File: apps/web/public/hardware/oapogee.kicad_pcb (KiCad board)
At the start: 2 copper layers, 22 x 60 mm, 27 parts, among them J1 USB-C-16P, J2 S2B-PH-K-S, J3 ANT-902-928, SW1 ARM-SWITCH, U1 MCP73831, U2 TODO-BUCK-BOOST, U3 RP2350A, U4 W25Q128JVSIQ, U5 BMP390, U6 ICM-42688-P, U7 ADXL375, U8 SX1262, U9 MAX-M10S

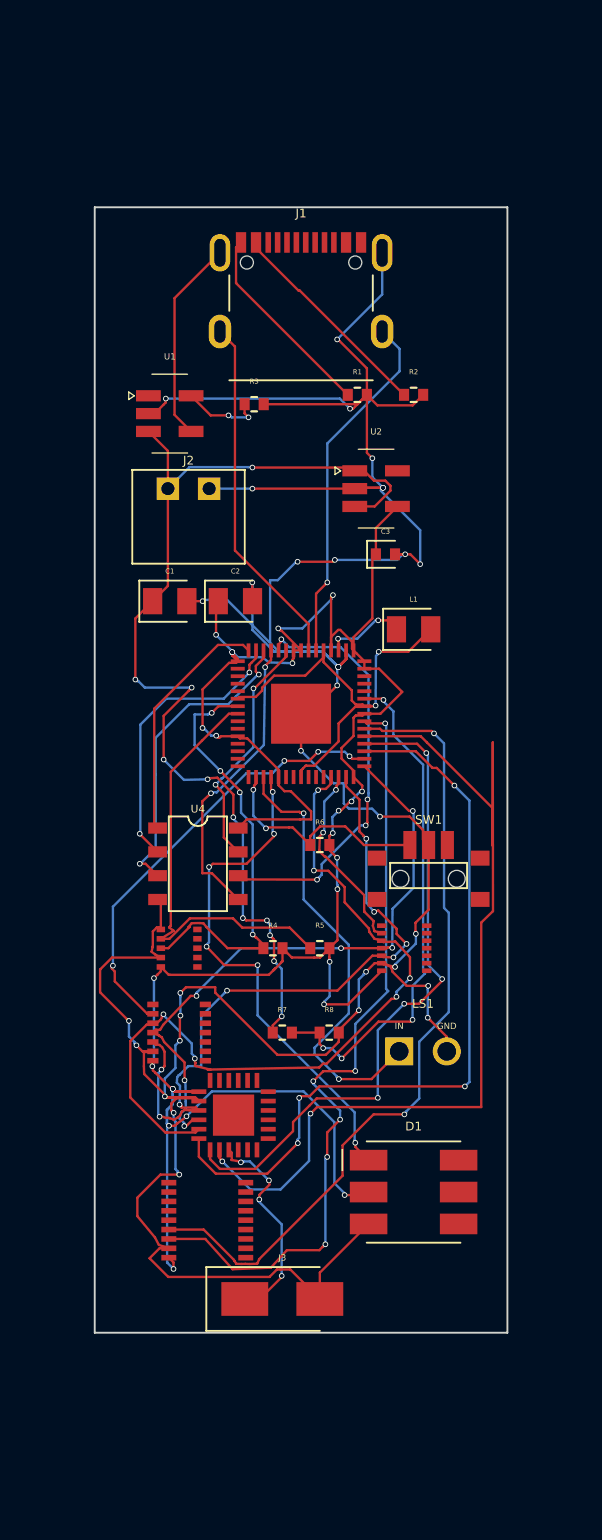
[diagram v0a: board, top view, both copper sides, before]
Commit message: The board could be flashed once and then never again
A page verification pass across the whole site found a hardware defect, which is
not where I expected one to come from.

RUN, SWCLK and SWDIO were all NOT_CONNECTED in the generated netlist, and
QSPI_CS went only to the flash. There is no dedicated bootloader pin on this
microcontroller: holding the flash chip select low as the chip leaves reset is
what selects USB boot. So a fabricated board could have been programmed exactly
once, while its flash was still blank and the bootrom fell through to USB, and
after that there would have been no way into the bootloader, no way to reset it,
and no way to attach a debugger. For a payload meant to be reflashed between
flights that is fatal, and I published Gerbers for it.

It was invisible in the schematic because the pins were simply absent, and
invisible to every check because nothing asserts that a microcontroller can be
programmed. Three pages meanwhile told the reader to "hold the boot button",
which is how it was caught: an instruction referring to a part that does not
exist.

The board now has SW2 on the flash chip select, SW3 on RUN, R9 pulling RUN up,
and three SWD pads. Press and hold boot, tap reset, release boot. It still
routes: 31 components, 108 traces, 152 vias, no missing traces, no unconnected
ports, no placement errors, and the fabrication package regenerated. The build
guide, the firmware page and the troubleshooting entry now describe what those
buttons actually do, including that a blank board enumerates on its own so the
first flash works even with an unsoldered button, which is exactly the sort of
thing that hides a missing part until the second flash.

The schematic page carried a red callout saying the pin numbers were structural
placeholders and "do not send anything here to a fabricator", twenty lines above
a Files tab offering the Gerbers and a heading saying the board can be ordered.
Both cannot be true. The pin numbers stopped being placehold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
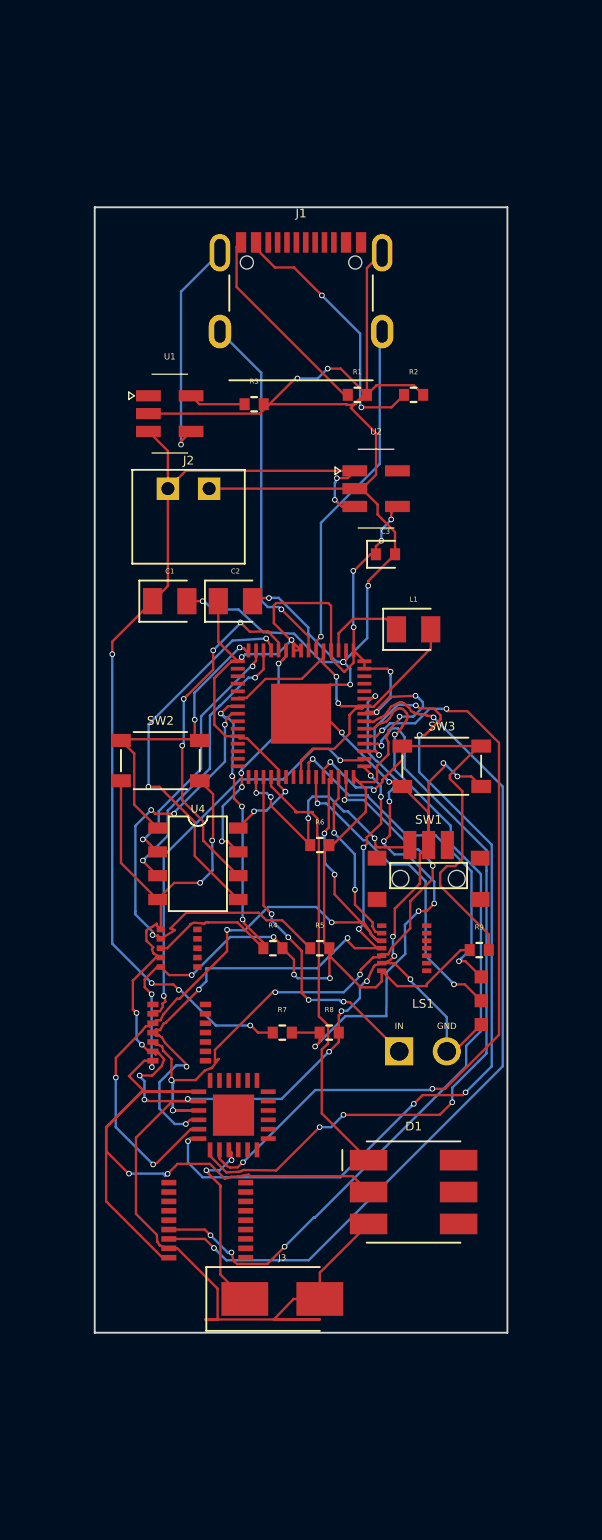
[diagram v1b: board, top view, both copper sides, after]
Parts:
- added J4: SWD-PADS, tscircuit:SWD-PADS, F.Cu at (109.6, 112.3)
- added R9: 10kΩ, tscircuit:resistor_res0402, F.Cu at (109.5, 109.6)
- added SW2: BOOT-BUTTON, tscircuit:BOOT-BUTTON, F.Cu at (92.5, 99.5)
- added SW3: RESET-BUTTON, tscircuit:RESET-BUTTON, F.Cu at (107.5, 99.8)
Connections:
- net .U3 .QSPI_CS to .U4 .CS renamed .SW2 .A1 to .U3 .QSPI_CS
- U3 pad 24: (no net) -> .J4 .SWCLK to .U3 .SWCLK
- U3 pad 25: (no net) -> .J4 .SWDIO to .U3 .SWDIO
- U3 pad 26: (no net) -> .SW3 .A1 to .U3 .RUN
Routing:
- net .SW3 .A1 to .U3 .RUN: track 0.00 -> 24.9 mm, vias 0 -> 2
- net .J4 .SWCLK to .U3 .SWCLK: track 0.00 -> 18.6 mm, vias 0 -> 2
- net .J4 .SWDIO to .U3 .SWDIO: track 0.00 -> 16.9 mm, vias 0 -> 2
- net V3V3: track 125.5 -> 141.0 mm, vias 24 -> 20
- net .U3 .RADIO_DIO1 to .U8 .DIO1: track 54.0 -> 42.6 mm, vias 2 -> 4
- net .U3 .CS_RADIO to .U8 .NSS: track 40.9 -> 48.4 mm, vias 4 -> 6
- net .U3 .BUZZER to .LS1 .IN: track 23.7 -> 18.8 mm, vias 2 -> 4
- net .U3 .GNSS_RX to .U9 .TXD: track 42.2 -> 47.0 mm, vias 6 -> 2
- net .U3 .RADIO_BUSY to .U8 .BUSY: track 35.6 -> 40.3 mm
- net .U3 .QSPI_D0 to .U4 .DI: track 16.1 -> 20.5 mm
- net .U3 .LED to .D1 .DIN: track 27.7 -> 23.8 mm, vias 6 -> 0
- net .U3 .QSPI_SCK to .U4 .CLK: track 22.6 -> 19.0 mm
- net .SW2 .A1 to .U3 .QSPI_CS: track 13.0 -> 16.5 mm, vias 0 -> 2
- net GND: track 193.5 -> 196.7 mm, vias 34 -> 27
- net VBAT: track 56.5 -> 53.4 mm, vias 11 -> 6
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
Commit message: Choose the regulator, and find out the board had outgrown itself
U2 was manufacturerPartNumber="TODO-BUCK-BOOST" on a five pin SOT-23, which is a
placeholder standing in for the part that feeds everything else. It is a
TPS63001 now, and every figure behind that choice comes from TI's datasheet
SLVS520C rather than from memory: 1.8 V to 5.5 V in, which spans a single
lithium cell from full charge to cutoff; fixed 3.3 V out, so there is no
feedback divider and no resistor pair to get wrong; up to 800 mA; 40 uA typical
quiescent at no load; VSON-10, 3 by 3 mm, exposed pad to PGND; one external
2.2 uH inductor, which is now L2.

Quiescent current decided it rather than efficiency at load. This payload sits
armed on a pad and then beeps in a field, both at almost no draw, so standing
loss is what sets how long it keeps beeping.

The schematic carries the datasheet's own pin numbering, the pad tied to PGND,
FB tied to VOUT as fixed-output parts require, and PS/SYNC grounded to enable
power-save, which is the mode that matters for a payload spending hours near
zero load.

Choosing it exposed something else. Adding eleven pads and two parts to a 22 by
60 mm board took the autorouter from seconds to over ten minutes, and then to
not finishing at all: a run was killed after forty-three minutes still working
on the schematic export. That is not a slow build, it is a build that cannot be
relied on to complete. The board is 28 by 78 mm with the placement spread to
match, which routes in under a minute, and the closest copper improved from
0.108 to 0.115 mm and the closest copper to a board edge from 0.72 to 1.34 mm as
a side effect. 32 components, 115 traces, 153 vias, nothing missing, nothing
unconnected, no placement errors, and the fabrication package regenerated. It
still fits the BT-55 sled, with 1.85 mm of rail each side instead of 0.6.

Also decided: the status LED is three plain LEDs, not an addressable one. The
WS2812 family wants a supply above the only rail this board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
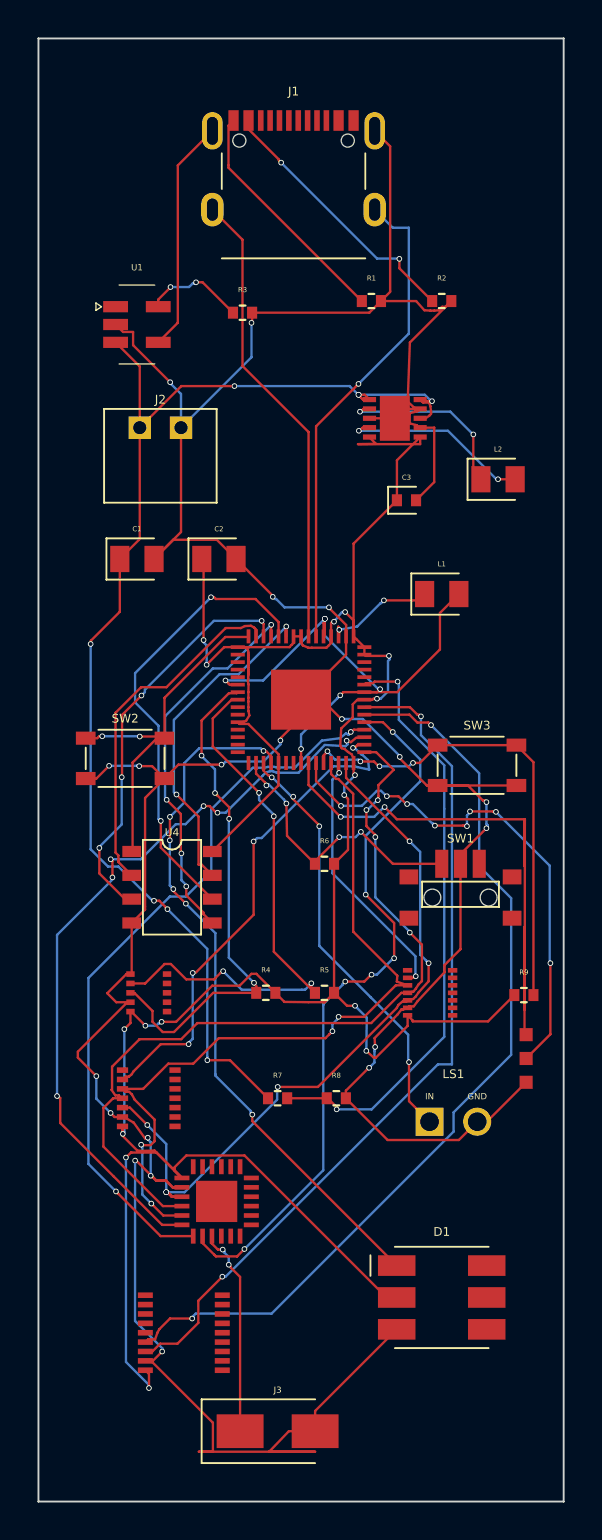
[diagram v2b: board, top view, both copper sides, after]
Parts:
- added L2: 2.2µH, tscircuit:inductor_0805, F.Cu at (110.5, 84.5)
- U2: value TODO-BUCK-BOOST -> TPS63001; footprint tscircuit:TODO-BUCK-BOOST -> tscircuit:TPS63001
- moved J3 7.05 mm to (98.8, 135.2)
- moved J1 6.51 mm to (99.6, 67.9)
- moved U9 6.13 mm to (93.8, 130.0)
- moved D1 5.82 mm to (107.5, 128.1)
- moved R2 5.22 mm to (107.5, 75.0)
- moved U1 5.06 mm to (91.2, 76.2)
- moved R1 5.06 mm to (103.8, 75.0)
- moved R3 4.92 mm to (96.9, 75.6)
- moved U8 4.69 mm to (95.5, 123.0)
- moved LS1 4.08 mm to (108.1, 118.8)
- moved J4 3.90 mm to (112.0, 115.4)
- moved U2 3.88 mm to (105.0, 81.2)
- moved U7 3.86 mm to (91.9, 117.5)
- moved J2 3.58 mm to (92.5, 81.8)
- moved R8 3.52 mm to (101.9, 117.5)
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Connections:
- U2 pad 1: VBAT -> V3V3
- U2 pad 2: GND -> .U2 .L2 to .L2 .pin2
- U2 pad 3: VBAT -> GND
- U2 pad 4: V3V3 -> .U2 .L1 to .L2 .pin1
- U2 pad 5: (no net) -> VBAT
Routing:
- net .J4 .SWCLK to .U3 .SWCLK: track 18.6 -> 39.2 mm
- net VBAT: track 53.4 -> 67.9 mm, vias 6 -> 8
- net .U3 .LED to .D1 .DIN: track 23.8 -> 37.6 mm, vias 0 -> 6
- net GND: track 196.7 -> 210.4 mm, vias 27 -> 20
- net .J4 .SWDIO to .U3 .SWDIO: track 16.9 -> 27.8 mm, vias 2 -> 8
- net .U2 .L2 to .L2 .pin2: track 0.00 -> 10.0 mm, vias 0 -> 2
- net .U2 .L1 to .L2 .pin1: track 0.00 -> 9.67 mm, vias 0 -> 2
- net .U3 .SPI_MOSI to .U6 .SDI: track 34.8 -> 44.4 mm, vias 8 -> 4
- net .J1 .DM to .U3 .USB_DM: track 18.5 -> 26.1 mm
- net .U3 .CS_RADIO to .U8 .NSS: track 48.4 -> 41.0 mm
- net VCORE: track 22.4 -> 29.5 mm, vias 2 -> 6
- net .U3 .QSPI_D2 to .U4 .WP: track 15.2 -> 21.7 mm, vias 2 -> 4
- net .U3 .SDA to .U5 .SDA: track 21.4 -> 27.1 mm
- net .J1 .DP to .U3 .USB_DP: track 19.3 -> 24.9 mm, vias 1 -> 0
- net .U3 .QSPI_SCK to .U4 .CLK: track 19.0 -> 24.4 mm, vias 4 -> 2
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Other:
- board size 22 x 60 mm -> 28 x 78 mm

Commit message: Replace the addressable LED, and catch the export lying about it
The status LED is three plain dice in one package now, driven by three pins
through three resistors, rather than an addressable part on one. The reason is
in the bill of materials: the WS2812 family wants a supply above the only rail
this board has, and a part run under its minimum works for whoever tested it and
does something else cold. One resistor per colour because the three dice do not
share a forward voltage, so a single shared one gives three brightnesses and no
way to fix one without moving the others.

Doing it exposed something worse than the LED.

Renaming three pins on the microcontroller left a stale entry in its schematic
pin arrangement, which still named the old label. tscircuit could not resolve
it, and the whole chip failed to create. The export printed success and exited
zero. The netlist came out with 64 of its 123 traces, missing every connection
that touches the microcontroller, and check-pcb reported a clean board: nothing
was unrouted, because the traces that would have been unrouted no longer
existed. I nearly committed a fabrication package for a board with no
microcontroller connected to anything.

Two checks now stand in front of that. Source errors are read before anything
else, because a netlist missing half its connections is not a board with a
routing problem, it is not the board. And the number of traces declared in the
circuit source is compared against the number that reached the netlist, since a
selector that resolves to nothing removes a connection without removing a line
of source, which is invisible to every other measurement. Both are blockers.

The board is 35 components, 119 routed traces, 195 vias, nothing missing,
nothing unconnected, no placement errors, fabrication package regenerated.
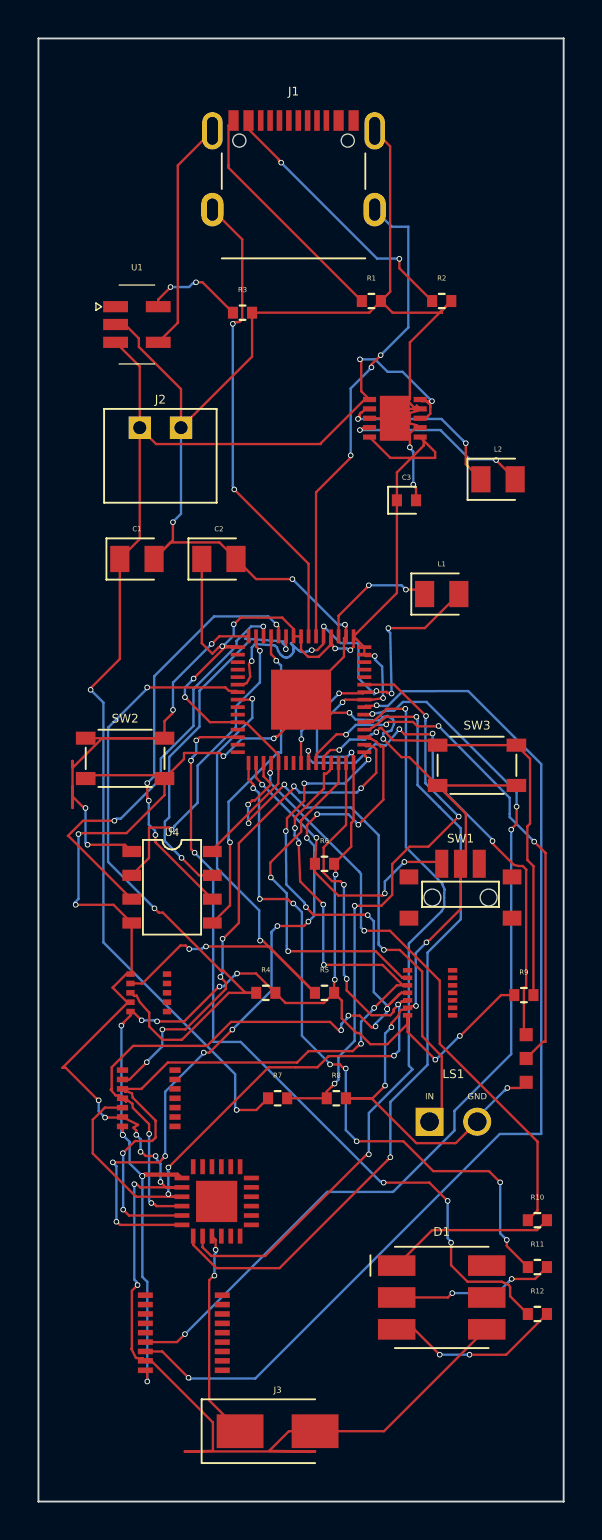
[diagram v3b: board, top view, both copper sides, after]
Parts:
- added R10: 330Ω, tscircuit:resistor_res0402, F.Cu at (112.6, 124.0)
- added R11: 220Ω, tscircuit:resistor_res0402, F.Cu at (112.6, 126.5)
- added R12: 220Ω, tscircuit:resistor_res0402, F.Cu at (112.6, 129.0)
- D1: value RGB-LED -> RGB-LED-CC; footprint tscircuit:RGB-LED -> tscircuit:RGB-LED-CC
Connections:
- D1 pad 1: .U3 .LED to .D1 .DIN -> .R10 .pin2 to .D1 .A_R
- D1 pad 2: V3V3 -> .R11 .pin2 to .D1 .A_G
- D1 pad 3: GND -> .R12 .pin2 to .D1 .A_B
- D1 pad 4: (no net) -> GND
- U3 pad 13: (no net) -> .U3 .LED_B to .R12 .pin1
- U3 pad 16: (no net) -> .U3 .LED_G to .R11 .pin1
- U3 pad 19: .U3 .LED to .D1 .DIN -> .U3 .LED_R to .R10 .pin1
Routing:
- net .U3 .LED_B to .R12 .pin1: track 0.00 -> 43.9 mm, vias 0 -> 6
- net .U3 .LED to .D1 .DIN: track 37.6 -> 0.00 mm, vias 6 -> 0
- net .U3 .LED_G to .R11 .pin1: track 0.00 -> 37.5 mm, vias 0 -> 8
- net .U3 .LED_R to .R10 .pin1: track 0.00 -> 31.4 mm, vias 0 -> 2
- net .U3 .GNSS_RX to .U9 .TXD: track 45.8 -> 58.3 mm
- net .J4 .SWCLK to .U3 .SWCLK: track 39.2 -> 27.2 mm, vias 2 -> 4
- net V3V3: track 145.0 -> 133.6 mm, vias 16 -> 24
- net .R12 .pin2 to .D1 .A_B: track 0.00 -> 9.47 mm, vias 0 -> 2
- net GND: track 210.4 -> 219.6 mm, vias 20 -> 24
- net .R10 .pin2 to .D1 .A_R: track 0.00 -> 9.01 mm
- net .R11 .pin2 to .D1 .A_G: track 0.00 -> 8.68 mm, vias 0 -> 2
- net .SW2 .A1 to .U3 .QSPI_CS: track 19.3 -> 27.9 mm, vias 2 -> 4
- net .U3 .SDA to .U5 .SDA: track 27.1 -> 35.2 mm, vias 4 -> 2
- net .U3 .BUZZER to .LS1 .IN: track 22.9 -> 30.5 mm
- net .U3 .SPI_MOSI to .U6 .SDI: track 44.4 -> 51.3 mm, vias 4 -> 12
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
